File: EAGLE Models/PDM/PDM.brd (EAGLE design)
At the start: 130.5 x 103.6 mm, 20 parts

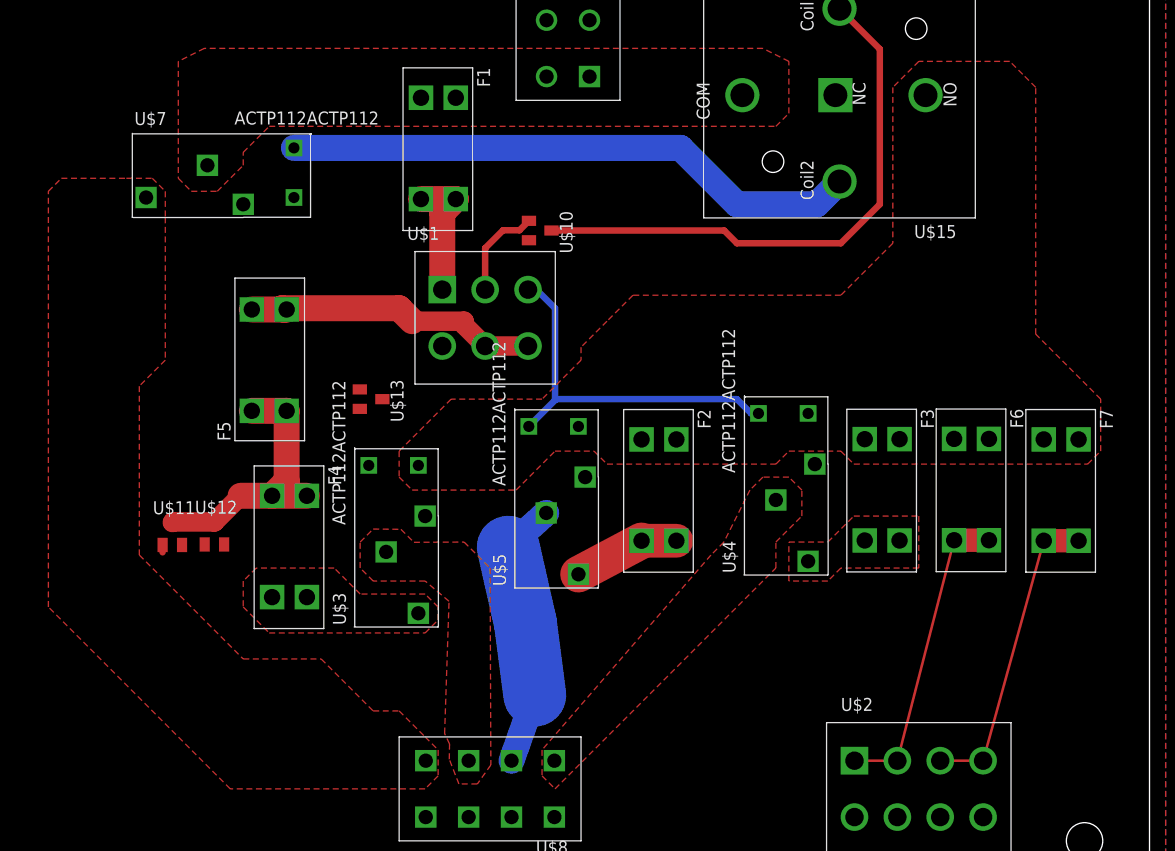
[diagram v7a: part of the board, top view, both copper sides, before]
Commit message: Completed Board Layout for main relay pdm
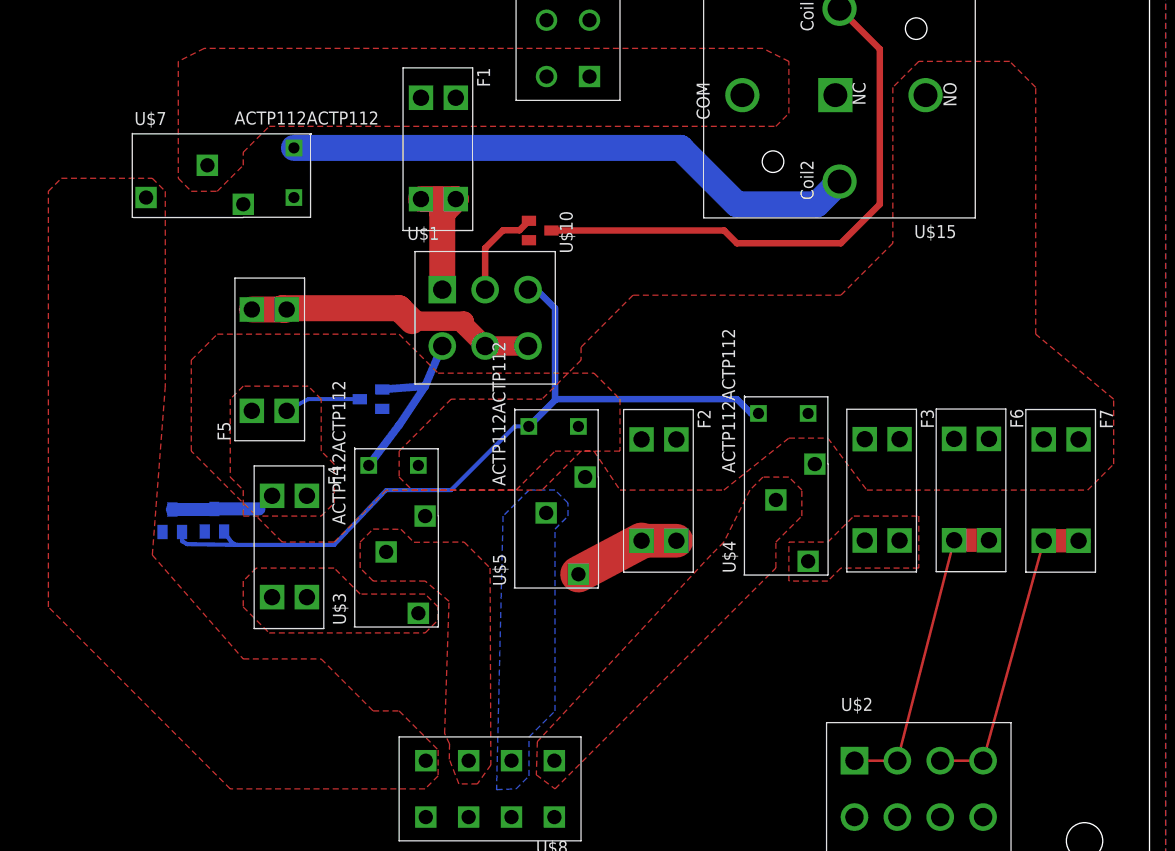
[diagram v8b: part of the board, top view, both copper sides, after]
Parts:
- moved U$11 1.27 mm to (35.0, 37.6), flipped to the bottom
- moved U$12 1.27 mm to (39.1, 37.7), flipped to the bottom
- flipped U$13 to the bottom
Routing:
- net A24: track 37.2 -> 78.2 mm
- net FUEL: track 26.5 -> 0.00 mm
- net A23: track 0.61 -> 18.0 mm
- net 12V: track 26.5 -> 17.8 mm
- added copper zone on layer 16, net FUEL
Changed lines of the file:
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@@
 <element name="U$9" library="molex" package="15-97-8043" value="15-97-8043" x="73.66" y="83.82"/>
 <element name="U$10" library="diodes-inc" package="SOT23-3" value="MMBD4448H-7-F" x="70.9422" y="66.0146" rot="R270"/>
-<element name="U$11" library="diodes-inc" package="SOT23-3" value="MMBD4448H-7-F" x="34.9758" y="36.3728"/>
-<element name="U$12" library="diodes-inc" package="SOT23-3" value="MMBD4448H-7-F" x="39.0906" y="36.4236"/>
-<element name="U$13" library="diodes-inc" package="SOT23-3" value="MMBD4448H-7-F" x="54.4068" y="49.53" rot="R270"/>
+<element name="U$11" library="diodes-inc" package="SOT23-3" value="MMBD4448H-7-F" x="34.9758" y="37.6428" rot="MR0"/>
+<element name="U$12" library="diodes-inc" package="SOT23-3" value="MMBD4448H-7-F" x="39.0906" y="37.6936" rot="MR0"/>
+<element name="U$13" library="diodes-inc" package="SOT23-3" value="MMBD4448H-7-F" x="54.4068" y="49.53" rot="MR270"/>
 <element name="F1" library="Keystone" package="3568" value="3568" x="60.9854" y="74.041" rot="R270"/>
 <element name="U$15" library="relay" package="VCF4-1000" value="VCF4-1000" x="100.203" y="79.248" rot="R180"/>
@@
 <contactref element="U$1" pad="4"/>
 <contactref element="U$13" pad="1"/>
-<wire x1="54.61" y1="43.4848" x2="54.1782" y2="43.053" width="0.635" layer="1"/>
-<wire x1="53.3068" y1="50.48" x2="61.3664" y2="54.7243" width="0" layer="19" extent="1-1"/>
-<wire x1="54.61" y1="43.4848" x2="53.3068" y2="50.48" width="0" layer="19" extent="1-1"/>
+<wire x1="61.3664" y1="54.7243" x2="59.69" y2="50.8" width="0.762" layer="16"/>
+<wire x1="59.69" y1="50.8" x2="55.5068" y2="50.48" width="0.762" layer="16"/>
+<wire x1="54.1782" y1="43.053" x2="57.15" y2="46.99" width="0.762" layer="16"/>
+<wire x1="57.15" y1="46.99" x2="59.69" y2="50.8" width="0.762" layer="16"/>
 </signal>
 <signal name="IGN_12V">
@@
 <wire x1="72.39" y1="58.42" x2="72.39" y2="49.53" width="0.635" layer="16"/>
 <wire x1="72.39" y1="49.53" x2="72.4408" y2="49.4792" width="0.635" layer="16"/>
-<wire x1="34.0258" y1="35.2728" x2="34.0258" y2="34.5542" width="0.635" layer="1"/>
-<wire x1="38.1406" y1="35.3236" x2="69.8246" y2="46.863" width="0" layer="19" extent="1-1"/>
-<wire x1="34.0258" y1="35.2728" x2="38.1406" y2="35.3236" width="0" layer="19" extent="1-1"/>
+<wire x1="69.8246" y1="46.863" x2="68.453" y2="46.863" width="0.4064" layer="16"/>
+<wire x1="68.453" y1="46.863" x2="62.23" y2="40.64" width="0.4064" layer="16"/>
+<wire x1="62.23" y1="40.64" x2="55.88" y2="40.64" width="0.4064" layer="16"/>
+<wire x1="55.88" y1="40.64" x2="50.8" y2="35.2806" width="0.4064" layer="16"/>
+<wire x1="50.8" y1="35.2806" x2="41.3004" y2="35.2806" width="0.4064" layer="16"/>
+<wire x1="41.2496" y1="35.2806" x2="41.125" y2="35.2806" width="0.4064" layer="16"/>
+<wire x1="41.125" y1="35.2806" x2="40.7047" y2="35.5993" width="0.4064" layer="16"/>
+<wire x1="40.7047" y1="35.5993" x2="40.0406" y2="36.5936" width="0.4064" layer="16"/>
+<wire x1="35.9258" y1="36.5428" x2="35.9258" y2="36.4642" width="0.4064" layer="16"/>
+<wire x1="35.9258" y1="36.5428" x2="35.9258" y2="35.6514" width="0.4064" layer="16"/>
+<wire x1="35.9258" y1="35.6514" x2="36.4236" y2="35.3568" width="0.4064" layer="16"/>
+<wire x1="36.4236" y1="35.3568" x2="41.3004" y2="35.2806" width="0.4064" layer="16"/>
+<wire x1="41.3004" y1="35.2806" x2="41.2496" y2="35.2806" width="0.4064" layer="16"/>
 </signal>
 <signal name="FAN">
@@
 <polygon width="0.635" layer="1" isolate="0.254">
 <vertex x="87.63" y="34.29"/>
-<vertex x="71.12" y="15.24"/>
-<vertex x="71.12" y="12.7"/>
+<vertex x="70.6628" y="16.0528"/>
+<vertex x="70.5612" y="12.8016"/>
 <vertex x="72.39" y="11.43"/>
 <vertex x="93.98" y="33.02"/>
@@
 <contactref element="U$5" pad="NO"/>
 <contactref element="U$8" pad="3"/>
-<wire x1="71.5264" y1="38.4048" x2="67.818" y2="35.052" width="2.54" layer="16"/>
-<wire x1="67.818" y1="35.052" x2="69.4944" y2="27.6352" width="6.1468" layer="16"/>
-<wire x1="69.4944" y1="27.6352" x2="70.4088" y2="20.5994" width="6.1468" layer="16"/>
-<wire x1="70.4088" y1="20.5994" x2="68.1355" y2="14.1859" width="2.54" layer="16"/>
+<polygon width="0.4064" layer="16" isolate="0.4064">
+<vertex x="67.31" y="38.1"/>
+<vertex x="66.675" y="11.3538"/>
+<vertex x="68.58" y="11.43"/>
+<vertex x="69.85" y="12.7"/>
+<vertex x="69.85" y="16.51"/>
+<vertex x="72.39" y="19.05"/>
+<vertex x="72.39" y="36.83"/>
+<vertex x="73.66" y="38.1"/>
+<vertex x="73.66" y="39.37"/>
+<vertex x="72.39" y="40.64"/>
+<vertex x="69.85" y="40.64"/>
+</polygon>
 </signal>
 <signal name="RECTIFIER">
@@
 <contactref element="U$8" pad="1"/>
 <polygon width="0.635" layer="1" isolate="0.254">
-<vertex x="30.48" y="71.12"/>
+<vertex x="24.13" y="71.12"/>
 <vertex x="33.02" y="71.12"/>
 <vertex x="34.29" y="69.85"/>
-<vertex x="34.29" y="67.31"/>
-<vertex x="34.29" y="53.34"/>
-<vertex x="31.75" y="50.8"/>
-<vertex x="31.75" y="34.29"/>
+<vertex x="34.29" y="50.8"/>
+<vertex x="33.02" y="34.29"/>
 <vertex x="41.91" y="24.13"/>
 <vertex x="49.53" y="24.13"/>
 <vertex x="54.61" y="19.05"/>
 <vertex x="57.15" y="19.05"/>
-<vertex x="59.69" y="16.51"/>
 <vertex x="60.96" y="15.24"/>
 <vertex x="60.96" y="12.7"/>
@@
 <vertex x="22.86" y="29.21"/>
 <vertex x="22.86" y="69.85"/>
-<vertex x="24.13" y="71.12"/>
 </polygon>
 </signal>
@@
 <contactref element="F7" pad="1"/>
 <polygon width="0.635" layer="1">
-<vertex x="100.33" y="44.45"/>
-<vertex x="101.6" y="43.18"/>
-<vertex x="124.46" y="43.18"/>
-<vertex x="125.73" y="44.45"/>
-<vertex x="125.73" y="49.53"/>
+<vertex x="99.06" y="45.72"/>
+<vertex x="102.87" y="40.64"/>
+<vertex x="124.46" y="40.64"/>
+<vertex x="127" y="43.18"/>
+<vertex x="127" y="49.53"/>
 <vertex x="119.38" y="55.88"/>
 <vertex x="119.38" y="80.01"/>
-<vertex x="118.11" y="81.28"/>
 <vertex x="116.84" y="82.55"/>
 <vertex x="107.95" y="82.55"/>
@@
 <vertex x="100.33" y="59.69"/>
 <vertex x="80.01" y="59.69"/>
-<vertex x="77.47" y="57.15"/>
 <vertex x="74.93" y="54.61"/>
 <vertex x="74.93" y="53.34"/>
@@
 <vertex x="72.39" y="44.45"/>
 <vertex x="76.2" y="44.45"/>
-<vertex x="77.47" y="43.18"/>
-<vertex x="93.98" y="43.18"/>
-<vertex x="95.25" y="44.45"/>
-</polygon>
-<wire x1="42.7482" y1="48.387" x2="46.1518" y2="48.387" width="2.54" layer="1"/>
-<wire x1="46.1518" y1="48.387" x2="46.1518" y2="41.5036" width="2.54" layer="1"/>
-<wire x1="46.1518" y1="41.5036" x2="44.7294" y2="40.0812" width="2.54" layer="1"/>
-<wire x1="48.133" y1="40.0812" x2="44.7294" y2="40.0812" width="2.54" layer="1"/>
-<wire x1="44.7294" y1="40.0812" x2="41.6482" y2="40.0812" width="2.54" layer="1"/>
-<wire x1="41.6482" y1="40.0812" x2="39.0906" y2="37.5236" width="1.905" layer="1"/>
-<wire x1="39.0906" y1="37.5236" x2="35.0266" y2="37.5236" width="1.905" layer="1"/>
-<wire x1="35.0266" y1="37.5236" x2="34.9758" y2="37.4728" width="1.905" layer="1"/>
-<wire x1="59.0296" y1="43.053" x2="55.5068" y2="49.53" width="0" layer="19" extent="1-1"/>
-<wire x1="46.1518" y1="48.387" x2="55.5068" y2="49.53" width="0" layer="19" extent="1-1"/>
+<vertex x="78.74" y="40.64"/>
+<vertex x="88.9" y="40.64"/>
+<vertex x="95.25" y="45.72"/>
+</polygon>
+<wire x1="34.9758" y1="38.7428" x2="39.0398" y2="38.7428" width="1.27" layer="16"/>
+<wire x1="39.0398" y1="38.7428" x2="39.0906" y2="38.7936" width="0.762" layer="16"/>
+<wire x1="39.0906" y1="38.7936" x2="43.4418" y2="38.7936" width="1.27" layer="16"/>
+<wire x1="43.4418" y1="38.7936" x2="44.7294" y2="40.0812" width="0.762" layer="16"/>
+<polygon width="0.762" layer="1">
+<vertex x="40.64" y="49.53"/>
+<vertex x="40.64" y="45.72"/>
+<vertex x="40.64" y="41.91"/>
+<vertex x="41.91" y="40.64"/>
+<vertex x="41.91" y="38.1"/>
+<vertex x="49.53" y="38.1"/>
+<vertex x="50.8" y="39.37"/>
+<vertex x="50.8" y="43.18"/>
+<vertex x="49.53" y="44.45"/>
+<vertex x="49.53" y="49.53"/>
+<vertex x="48.26" y="50.8"/>
+<vertex x="41.91" y="50.8"/>
+</polygon>
+<wire x1="53.3068" y1="49.53" x2="48.26" y2="49.53" width="0.381" layer="16"/>
+<wire x1="48.26" y1="49.53" x2="46.1518" y2="48.387" width="0.381" layer="16"/>
+<polygon width="0.381" layer="1">
+<vertex x="39.37" y="55.88"/>
+<vertex x="57.15" y="55.88"/>
+<vertex x="60.96" y="52.07"/>
+<vertex x="76.2" y="52.07"/>
+<vertex x="78.74" y="49.53"/>
+<vertex x="78.74" y="44.45"/>
+<vertex x="74.93" y="44.45"/>
+<vertex x="71.12" y="40.64"/>
+<vertex x="55.88" y="40.64"/>
+<vertex x="50.8" y="35.56"/>
+<vertex x="45.72" y="35.56"/>
+<vertex x="36.83" y="44.45"/>
+<vertex x="36.83" y="53.34"/>
+</polygon>
 </signal>
 <signal name="BAT_+12_FUSED">
